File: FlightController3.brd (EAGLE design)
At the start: 50.8 x 78.4 mm, 27 parts, among them U1 NUCLEO_L432KC

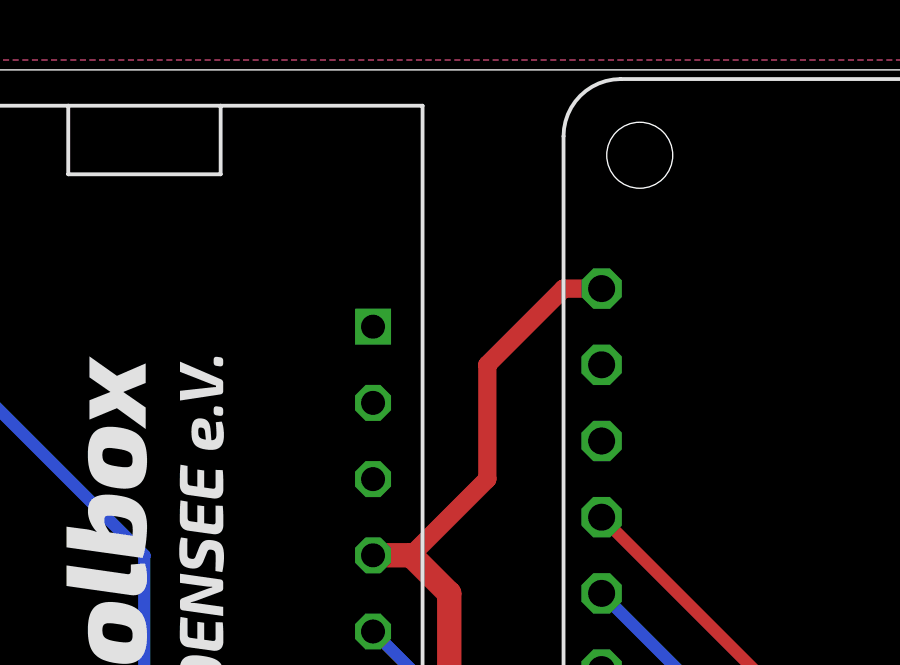
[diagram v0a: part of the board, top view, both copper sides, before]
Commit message: added reset header
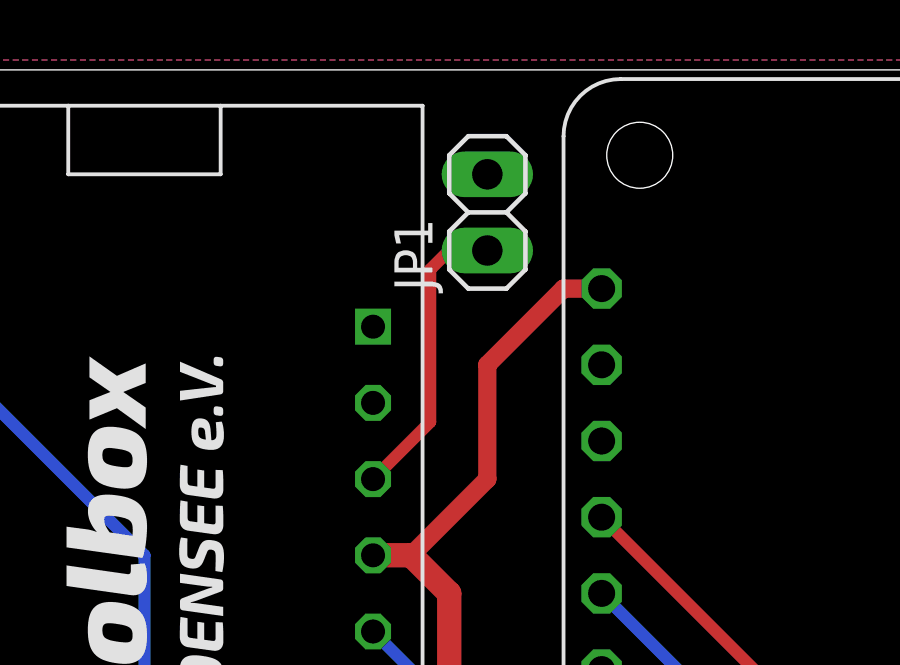
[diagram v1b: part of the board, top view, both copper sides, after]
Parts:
- added JP1: (no value), pinhead:1X02
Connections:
- new net !RST: JP1.1, U1.!RST, U1.2!RST
- net GND: now also JP1.2
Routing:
- net !RST: track 0.00 -> 9.94 mm
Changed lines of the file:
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@@
 <element name="C14" library="pinhead" package="1X04" value="" x="39.37" y="3.81" rot="R180"/>
 <element name="U$1" library="toolbox" package="TOOLBOX" value="TOOLBOX_LOGO" x="12.665" y="59.925" rot="R90"/>
+<element name="JP1" library="pinhead" package="1X02" value="" x="22.86" y="73.66" rot="R90"/>
 </elements>
 <signals>
@@
 <contactref element="C13" pad="2"/>
 <contactref element="C12" pad="2"/>
+<contactref element="JP1" pad="2"/>
 </signal>
 <signal name="VIN">
@@
 <wire x1="38.1" y1="10.16" x2="38.1" y2="3.81" width="0.4064" layer="1"/>
 </signal>
+<signal name="!RST">
+<contactref element="U1" pad="!RST" route="any" routetag="G$1.!RST"/>
+<contactref element="U1" pad="2!RST" route="any" routetag="G$1.!RST"/>
+<contactref element="JP1" pad="1"/>
+<wire x1="19.05" y1="64.77" x2="20.955" y2="66.675" width="0.4064" layer="1"/>
+<wire x1="20.955" y1="66.675" x2="20.955" y2="71.755" width="0.4064" layer="1"/>
+<wire x1="20.955" y1="71.755" x2="21.59" y2="72.39" width="0.4064" layer="1"/>
+<wire x1="21.59" y1="72.39" x2="22.86" y2="72.39" width="0.4064" layer="1"/>
+</signal>
 </signals>

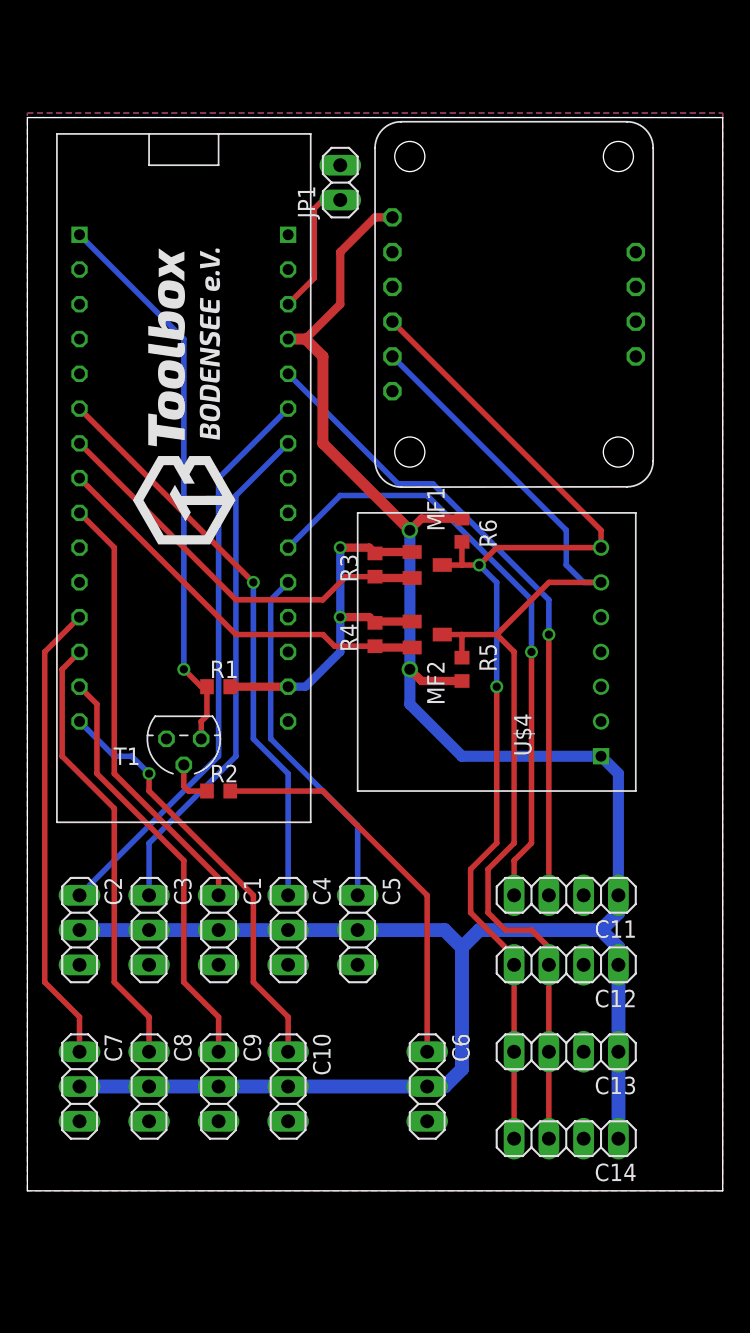
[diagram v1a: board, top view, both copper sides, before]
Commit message: added mounting holes, removed BNO-055 mounting holes
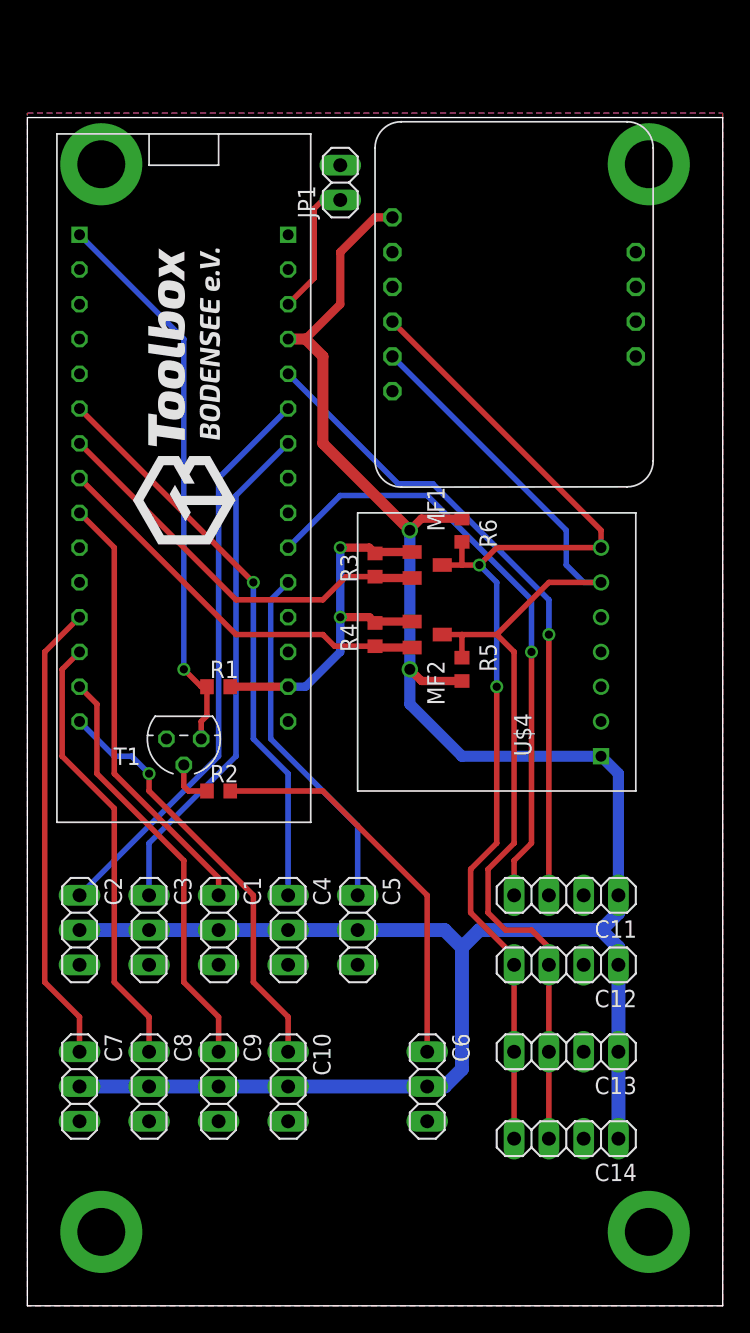
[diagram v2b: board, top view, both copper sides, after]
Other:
- board size 50.8 x 78.4 mm -> 50.8 x 86.8 mm
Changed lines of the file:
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@@
 <board>
 <plain>
-<wire x1="0" y1="0" x2="50.8" y2="0" width="0" layer="20"/>
-<wire x1="50.8" y1="0" x2="50.8" y2="78.41" width="0" layer="20"/>
+<wire x1="0" y1="-8.4" x2="50.8" y2="-8.4" width="0" layer="20"/>
+<wire x1="50.8" y1="-8.4" x2="50.8" y2="78.41" width="0" layer="20"/>
 <wire x1="50.8" y1="78.41" x2="0" y2="78.41" width="0" layer="20"/>
-<wire x1="0" y1="78.41" x2="0" y2="0" width="0" layer="20"/>
+<wire x1="0" y1="78.41" x2="0" y2="-8.4" width="0" layer="20"/>
 </plain>
 <attributes>
@@
 <vertex x="0" y="78.74"/>
 <vertex x="50.8" y="78.74"/>
-<vertex x="50.8" y="0"/>
-<vertex x="0" y="0"/>
+<vertex x="50.8" y="-8.4"/>
+<vertex x="0" y="-8.4"/>
 </polygon>
 <polygon width="0.4064" layer="16">
 <vertex x="0" y="78.74"/>
 <vertex x="50.8" y="78.74"/>
-<vertex x="50.8" y="0"/>
-<vertex x="0" y="0"/>
+<vertex x="50.8" y="-8.4"/>
+<vertex x="0" y="-8.4"/>
 </polygon>
 <contactref element="C14" pad="2"/>
@@
 <contactref element="C12" pad="2"/>
 <contactref element="JP1" pad="2"/>
+<via x="5.4" y="75" extent="1-16" drill="3.5" diameter="6"/>
+<via x="45.4" y="75" extent="1-16" drill="3.5" diameter="6"/>
+<via x="5.4" y="-3" extent="1-16" drill="3.5" diameter="6"/>
+<via x="45.4" y="-3" extent="1-16" drill="3.5" diameter="6"/>
 </signal>
 <signal name="VIN">

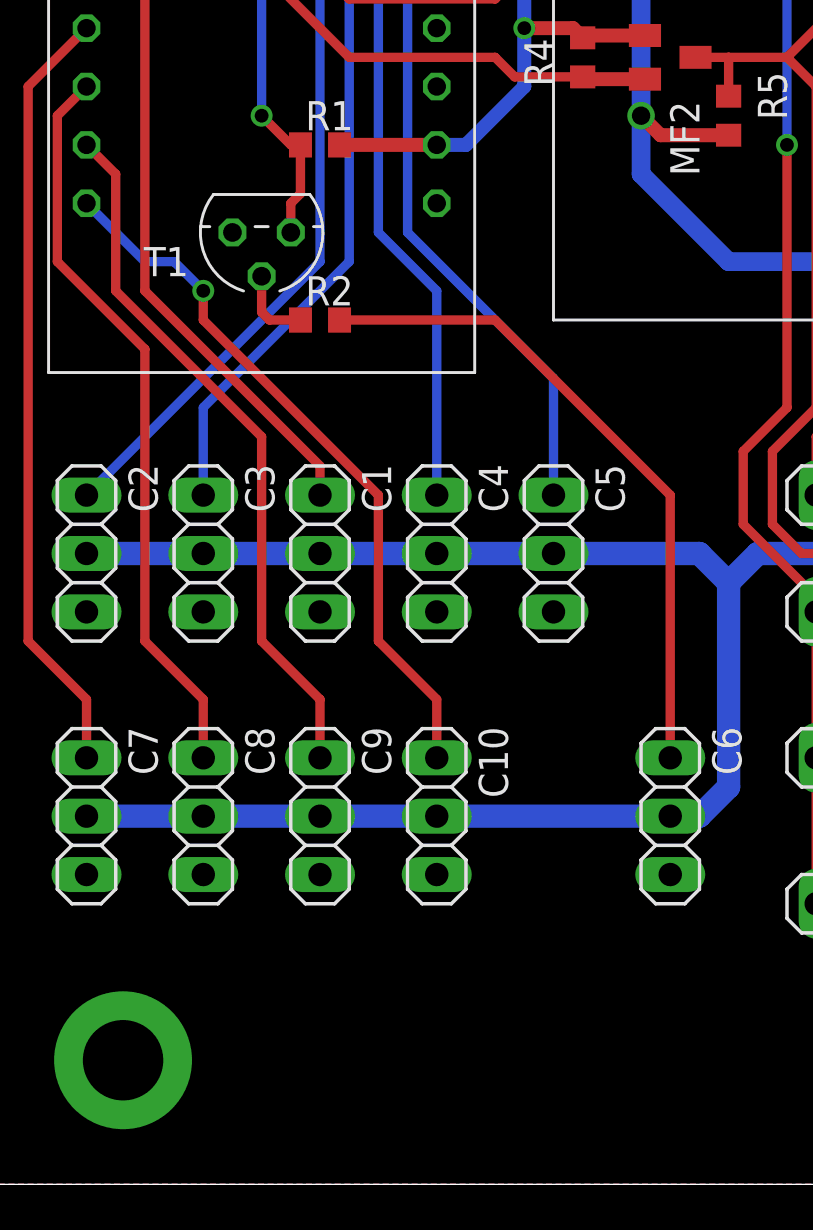
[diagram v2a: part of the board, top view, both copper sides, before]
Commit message: power LEDs
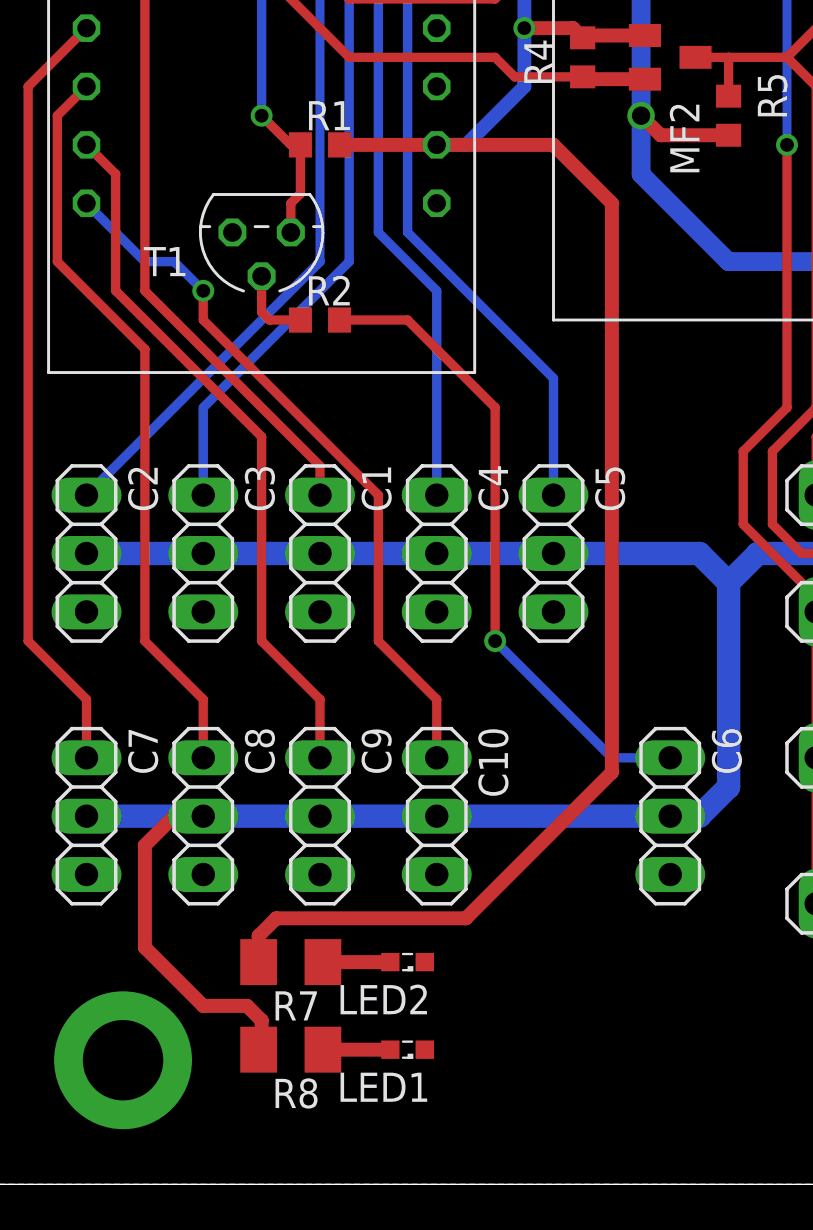
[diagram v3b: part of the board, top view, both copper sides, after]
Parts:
- added LED1, LED2: (no value), led:SML0603
- added R7: 110, resistor:M1206
- added R8: 150, resistor:M1206
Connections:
- new net N$2: LED2.A, R7.1
- new net N$3: LED1.A, R8.1
- net +3V3: now also R7.2
- net +5V: now also R8.2
- net GND: now also LED1.C, LED2.C
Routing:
- net +3V3: track 27.8 -> 80.7 mm
- net +5V: track 173.3 -> 188.5 mm
- net N$3: track 0.00 -> 2.93 mm
- net N$2: track 0.00 -> 2.93 mm
- net SBUS: track 29.0 -> 28.2 mm, vias 0 -> 1
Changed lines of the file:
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@@
 <element name="U$1" library="toolbox" package="TOOLBOX" value="TOOLBOX_LOGO" x="12.665" y="59.925" rot="R90"/>
 <element name="JP1" library="pinhead" package="1X02" value="" x="22.86" y="73.66" rot="R90"/>
+<element name="LED1" library="led" package="SML0603" value="" x="17.78" y="-2.54" rot="R180"/>
+<element name="LED2" library="led" package="SML0603" value="" x="17.78" y="1.27" rot="R180"/>
+<element name="R7" library="resistor" package="M1206" value="110" x="12.7" y="1.27" rot="R180"/>
+<element name="R8" library="resistor" package="M1206" value="150" x="12.7" y="-2.54" rot="R180"/>
 </elements>
 <signals>
@@
 <via x="5.4" y="-3" extent="1-16" drill="3.5" diameter="6"/>
 <via x="45.4" y="-3" extent="1-16" drill="3.5" diameter="6"/>
+<contactref element="LED2" pad="C"/>
+<contactref element="LED1" pad="C"/>
 </signal>
 <signal name="VIN">
@@
 <wire x1="27.94" y1="38.1" x2="28.79" y2="37.25" width="0.6096" layer="1"/>
 <wire x1="28.79" y1="37.25" x2="31.75" y2="37.25" width="0.6096" layer="1"/>
+<contactref element="R8" pad="2"/>
+<wire x1="8.89" y1="7.62" x2="7.62" y2="7.62" width="0.6096" layer="1"/>
+<wire x1="7.62" y1="7.62" x2="6.35" y2="6.35" width="0.6096" layer="1"/>
+<wire x1="6.35" y1="1.905" x2="8.89" y2="-0.635" width="0.6096" layer="1"/>
+<wire x1="8.89" y1="-0.635" x2="10.795" y2="-0.635" width="0.6096" layer="1"/>
+<wire x1="10.795" y1="-0.635" x2="11.43" y2="-1.27" width="0.6096" layer="1"/>
+<wire x1="11.43" y1="-1.27" x2="11.43" y2="-2.41" width="0.6096" layer="1"/>
+<wire x1="11.43" y1="-2.41" x2="11.3" y2="-2.54" width="0.6096" layer="1"/>
+<wire x1="6.35" y1="6.35" x2="6.35" y2="1.905" width="0.6096" layer="1"/>
 </signal>
 <signal name="PPM_MOTOR">
@@
 <contactref element="C6" pad="1"/>
 <contactref element="R2" pad="2"/>
-<wire x1="14.82" y1="29.21" x2="21.59" y2="29.21" width="0.4064" layer="1"/>
-<wire x1="21.59" y1="29.21" x2="29.21" y2="21.59" width="0.4064" layer="1"/>
-<wire x1="29.21" y1="21.59" x2="29.21" y2="10.16" width="0.4064" layer="1"/>
+<wire x1="29.21" y1="10.16" x2="26.67" y2="10.16" width="0.4064" layer="16"/>
+<wire x1="26.67" y1="10.16" x2="21.59" y2="15.24" width="0.4064" layer="16"/>
+<via x="21.59" y="15.24" extent="1-16" drill="0.6" shape="octagon"/>
+<wire x1="21.59" y1="25.4" x2="17.78" y2="29.21" width="0.4064" layer="1"/>
+<wire x1="17.78" y1="29.21" x2="14.82" y2="29.21" width="0.4064" layer="1"/>
+<wire x1="21.59" y1="15.24" x2="21.59" y2="25.4" width="0.4064" layer="1"/>
 </signal>
 <signal name="+3V3">
@@
 <wire x1="24.98" y1="46.99" x2="25.4" y2="46.57" width="0.6096" layer="1"/>
 <contactref element="U1" pad="+3V3"/>
-<wire x1="14.82" y1="36.83" x2="19.05" y2="36.83" width="0.6096" layer="1"/>
+<wire x1="19.05" y1="36.83" x2="14.82" y2="36.83" width="0.6096" layer="1"/>
 <wire x1="19.05" y1="36.83" x2="20.32" y2="36.83" width="0.6096" layer="16"/>
 <wire x1="20.32" y1="36.83" x2="22.86" y2="39.37" width="0.6096" layer="16"/>
 <wire x1="22.86" y1="39.37" x2="22.86" y2="41.91" width="0.6096" layer="16"/>
+<contactref element="R7" pad="2"/>
+<wire x1="11.3" y1="1.27" x2="11.3" y2="2.41" width="0.6096" layer="1"/>
+<wire x1="11.3" y1="2.41" x2="12.065" y2="3.175" width="0.6096" layer="1"/>
+<wire x1="12.065" y1="3.175" x2="20.32" y2="3.175" width="0.6096" layer="1"/>
+<wire x1="26.67" y1="34.29" x2="24.13" y2="36.83" width="0.6096" layer="1"/>
+<wire x1="24.13" y1="36.83" x2="19.05" y2="36.83" width="0.6096" layer="1"/>
+<wire x1="20.32" y1="3.175" x2="26.67" y2="9.525" width="0.6096" layer="1"/>
+<wire x1="26.67" y1="9.525" x2="26.67" y2="34.29" width="0.6096" layer="1"/>
 </signal>
 <signal name="NAVBOARD_TX">
@@
 <wire x1="21.59" y1="72.39" x2="22.86" y2="72.39" width="0.4064" layer="1"/>
 </signal>
+<signal name="N$2">
+<contactref element="R7" pad="1"/>
+<contactref element="LED2" pad="A"/>
+<wire x1="14.1" y1="1.27" x2="17.03" y2="1.27" width="0.6096" layer="1"/>
+</signal>
+<signal name="N$3">
+<contactref element="LED1" pad="A"/>
+<contactref element="R8" pad="1"/>
+<wire x1="14.1" y1="-2.54" x2="17.03" y2="-2.54" width="0.6096" layer="1"/>
+</signal>
 </signals>
